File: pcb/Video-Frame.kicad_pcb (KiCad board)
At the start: 4 copper layers, 80 x 50 mm, 121 parts, among them J1 POWER, J2 USB_B_Micro, J3 DBG_SWD, J4 Micro_SD_Card_Det, J5 DISPLAY, J6 USART3, SW1 BOOT, SW2 RESET, U1 MP2451DT, U2 SY6280A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

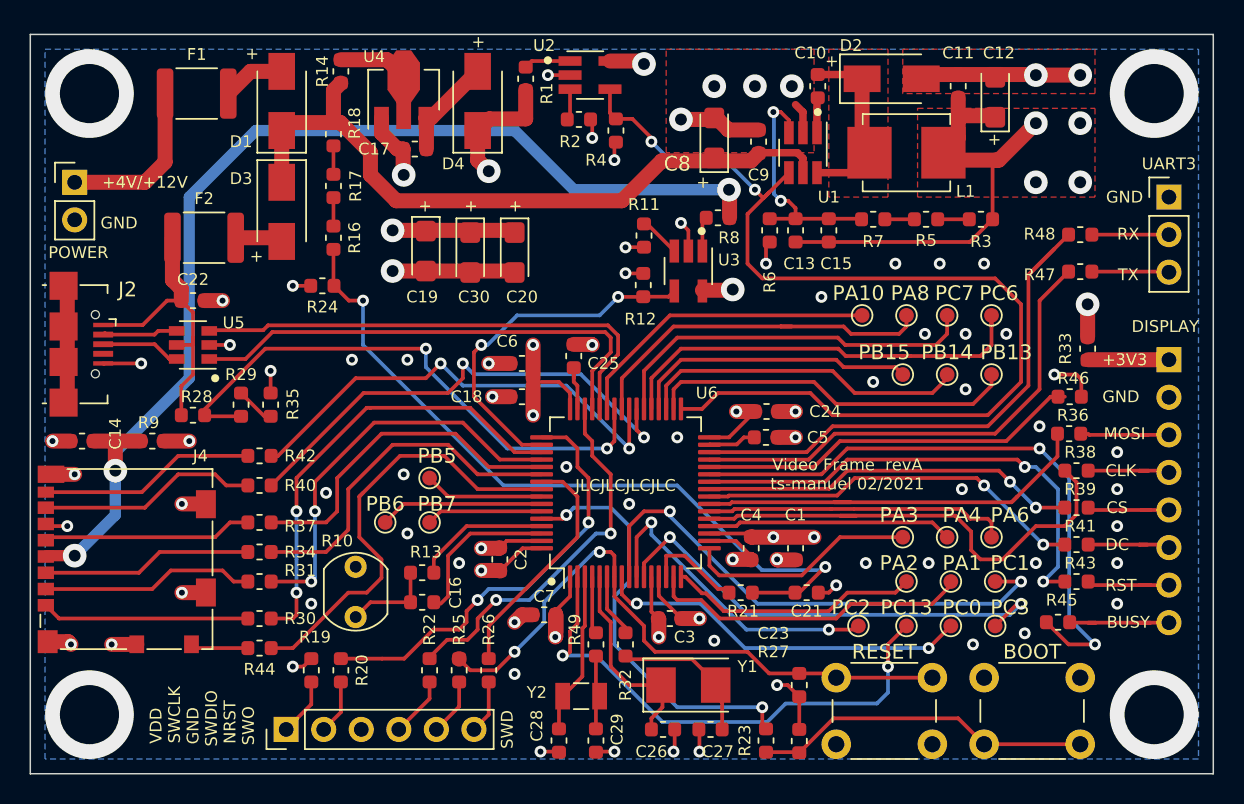
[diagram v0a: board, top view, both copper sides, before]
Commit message: Updated schematic and PCB Layout
Changes in schematic
+ Added super capacitor on VDD
+ Added notes
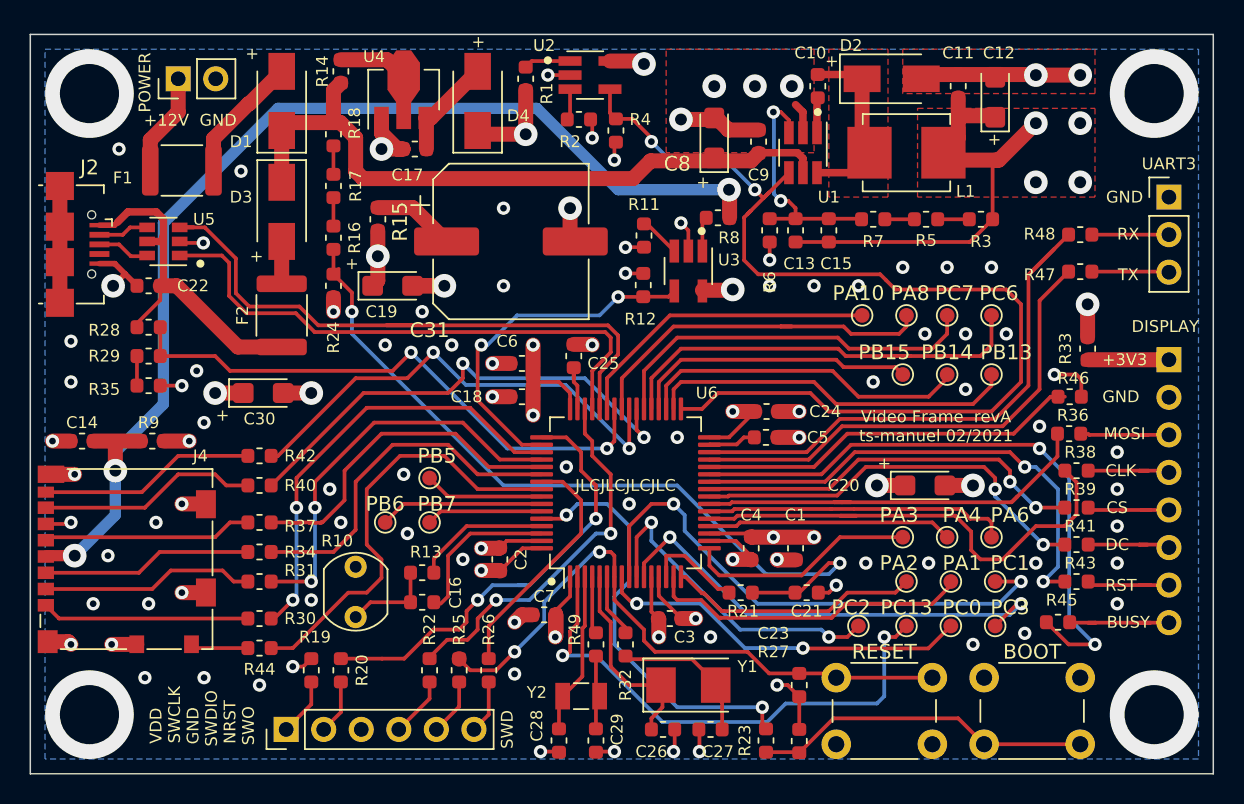
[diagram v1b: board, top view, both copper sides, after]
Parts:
- added C31: 47m, Capacitor_SMD:CP_Elec_10x7.7, F.Cu at (127.5, 89.0)
- added R15: 100Ω, Resistor_SMD:R_0603_1608Metric, F.Cu at (118.5, 87.5)
- moved C20 31.9 mm to (155.5, 105.5), turned to 0 degrees
- moved C30 16.9 mm to (110.8, 99.2), turned to 0 degrees
- moved J1 9.90 mm to (105.0, 78.0), turned to 90 degrees
- moved R35 8.35 mm to (103.0, 98.8), turned to 0 degrees
- moved F2 7.42 mm to (112.0, 94.0), turned to 90 degrees
- moved U5 7.28 mm to (104.0, 89.0)
- moved R29 7.06 mm to (103.0, 96.8), turned to 180 degrees
- moved J2 6.75 mm to (97.0, 88.0)
- moved R28 6.66 mm to (103.0, 94.8)
- moved F1 5.30 mm to (105.2, 84.2)
- moved C19 3.25 mm to (119.5, 92.0), turned to 0 degrees
- moved C22 3.16 mm to (103.0, 92.0), turned to 180 degrees
- moved R24 0.75 mm to (115.5, 92.0), turned to -90 degrees
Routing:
- net /USB_D-: track 33.6 -> 42.2 mm
- net Net-(C31-Pad1): track 0.00 -> 5.60 mm
- net Net-(D1-Pad2): track 4.23 -> 9.19 mm
- net /USB_D+: track 33.5 -> 38.1 mm
- net /VBUS: track 20.5 -> 24.5 mm
- net Net-(F1-Pad1): track 11.3 -> 7.53 mm
- net VDD: track 53.2 -> 50.3 mm, vias 11 -> 13
- net Net-(C21-Pad1): track 51.3 -> 53.6 mm
- net GND: track 98.4 -> 100.7 mm, vias 82 -> 102
- net Net-(J2-Pad2): track 5.32 -> 3.43 mm
- net Net-(J2-Pad3): track 5.39 -> 3.58 mm
- net /EP_DC: track 26.4 -> 27.8 mm
- net +3V3_SD: track 76.0 -> 77.3 mm
- net /EP_CS: track 25.6 -> 26.7 mm
- net /SWCLK: track 29.2 -> 30.1 mm
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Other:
- board text added: "+12V"
- board text removed: "+4V/+12V"
